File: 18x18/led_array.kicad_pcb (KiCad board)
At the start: 2 copper layers, 186 x 146 mm, 336 parts, among them M1 P***, M2 P***, M3 P***, M4 P***, P1 CONN_2, SW1 SWITCH_INV

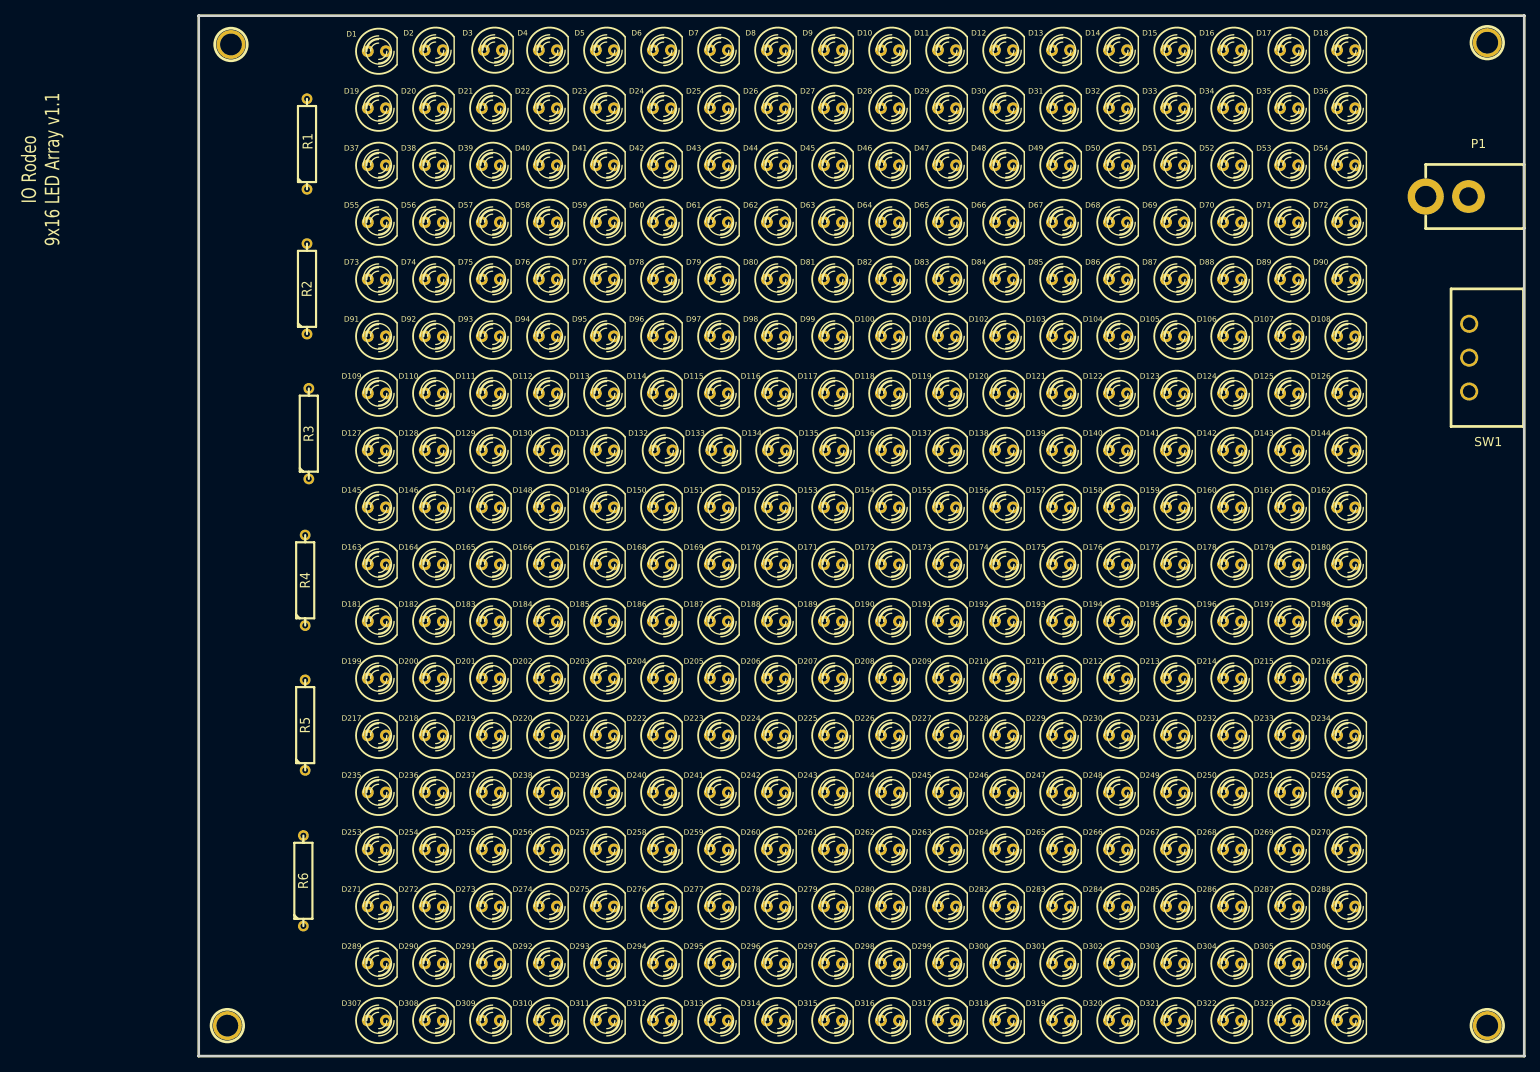
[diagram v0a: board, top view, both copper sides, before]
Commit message: Finished layout and routing of 9x18 and 18x18 led arrays.
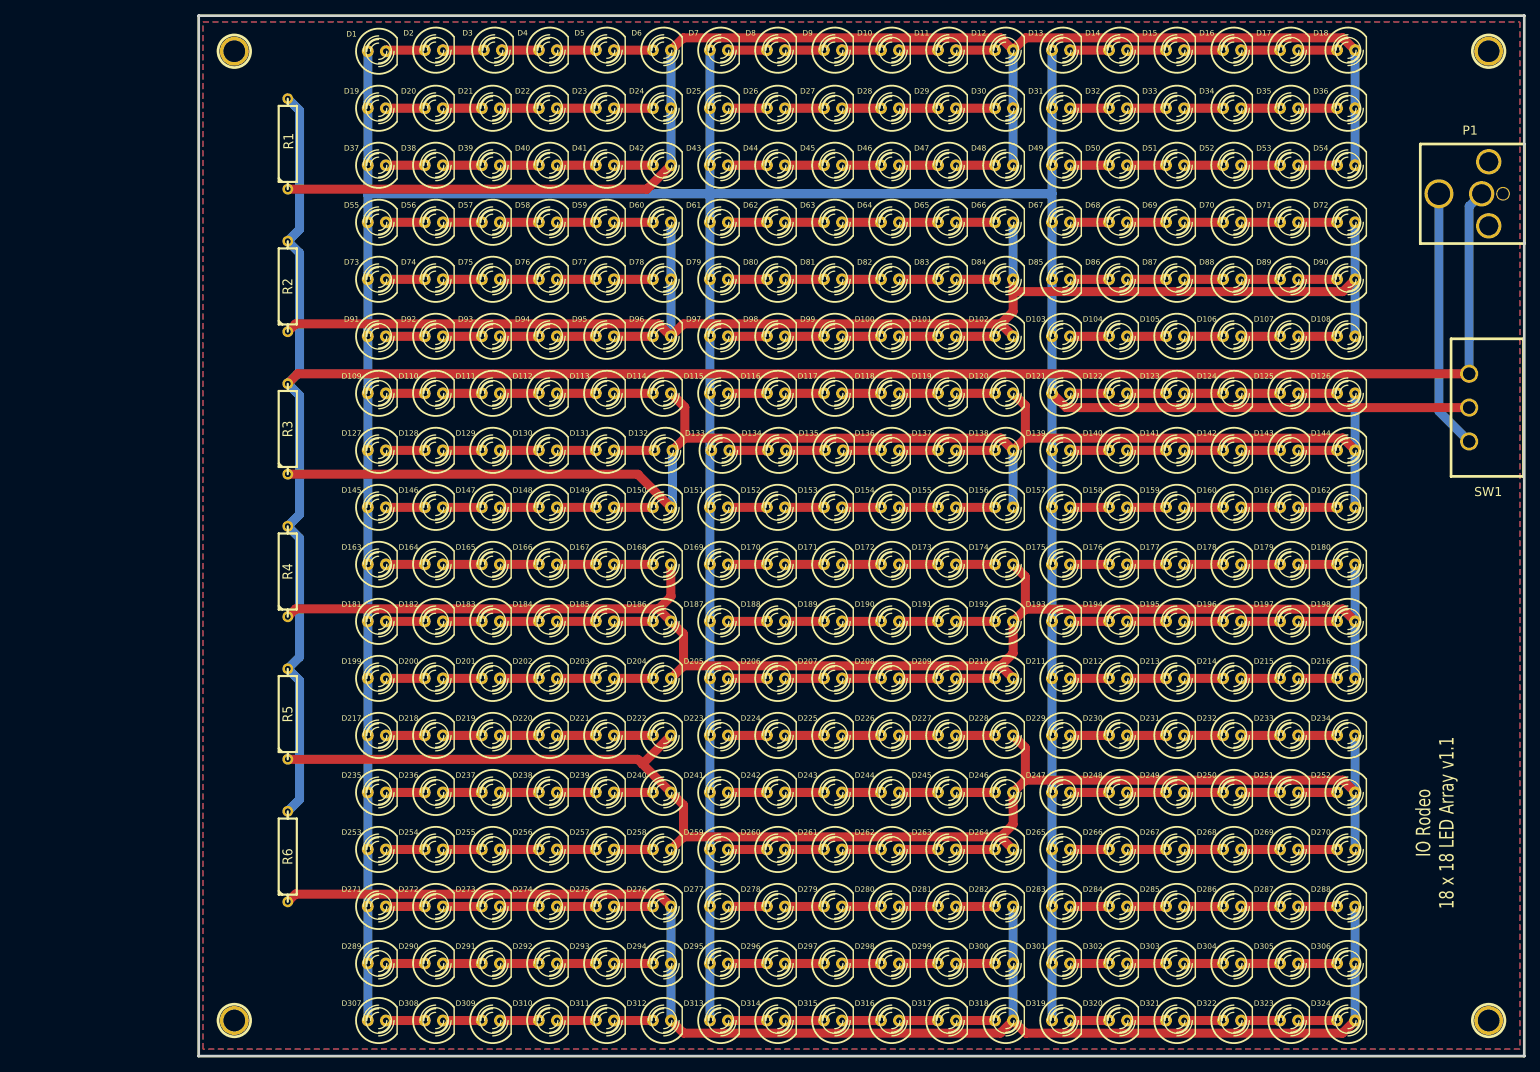
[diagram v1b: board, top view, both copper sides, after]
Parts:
- P1: footprint DCJACK_2PIN -> DCJACK_2PIN_HIGHCURRENT
- moved P1 13.8 mm to (247.0, 40.0), turned to 270 degrees
- moved SW1 7.01 mm to (241.8, 70.0)
- moved R6 4.04 mm to (73.5, 133.0)
- moved R3 3.03 mm to (73.5, 73.0)
- moved R5 2.90 mm to (73.5, 113.0)
- moved R4 2.74 mm to (73.5, 93.0)
- moved R2 2.72 mm to (73.5, 53.0)
- moved R1 2.70 mm to (73.5, 33.0)
- moved M3 1.22 mm to (242.0, 20.0)
- moved M4 1.21 mm to (66.0, 156.0)
- moved M1 1.06 mm to (66.0, 20.0)
- moved M2 0.74 mm to (242.0, 156.0)
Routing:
- net N-00000254: track 0.00 -> 563.8 mm
- net GND: track 0.00 -> 299.2 mm
- net N-00000197: track 0.00 -> 202.5 mm
- net N-00000105: track 0.00 -> 201.9 mm
- net N-00000249: track 0.00 -> 200.5 mm
- net N-00000257: track 0.00 -> 200.1 mm
- net N-0000061: track 0.00 -> 197.7 mm
- net N-00000119: track 0.00 -> 197.2 mm
- net /15V: track 0.00 -> 36.5 mm
- net N-00000212: track 0.00 -> 5.74 mm
- net N-00000250: track 0.00 -> 5.67 mm
- net N-00000213: track 0.00 -> 5.52 mm
- net N-0000099: track 0.00 -> 5.46 mm
- net N-0000098: track 0.00 -> 5.46 mm
- net N-0000097: track 0.00 -> 5.46 mm
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- added copper zone on B.Cu, net GND
- added copper zone on F.Cu, net GND
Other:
- net class Default: trace_width 0.762 -> 1.27
- board text added: "IO Rodeo 18 x 18 LED Array v1.1"
- board text removed: "IO Rodeo 9x16 LED Array v1.1"
